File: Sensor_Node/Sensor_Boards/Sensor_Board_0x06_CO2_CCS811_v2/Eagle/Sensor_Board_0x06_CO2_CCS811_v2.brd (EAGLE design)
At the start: 55 x 35 mm, 28 parts, among them J1 M04_SMD_90, J4 ARDUINO_ISP, U1 CCS811, U2 ATMEGA328P_TQFP, Y1 8MHZ

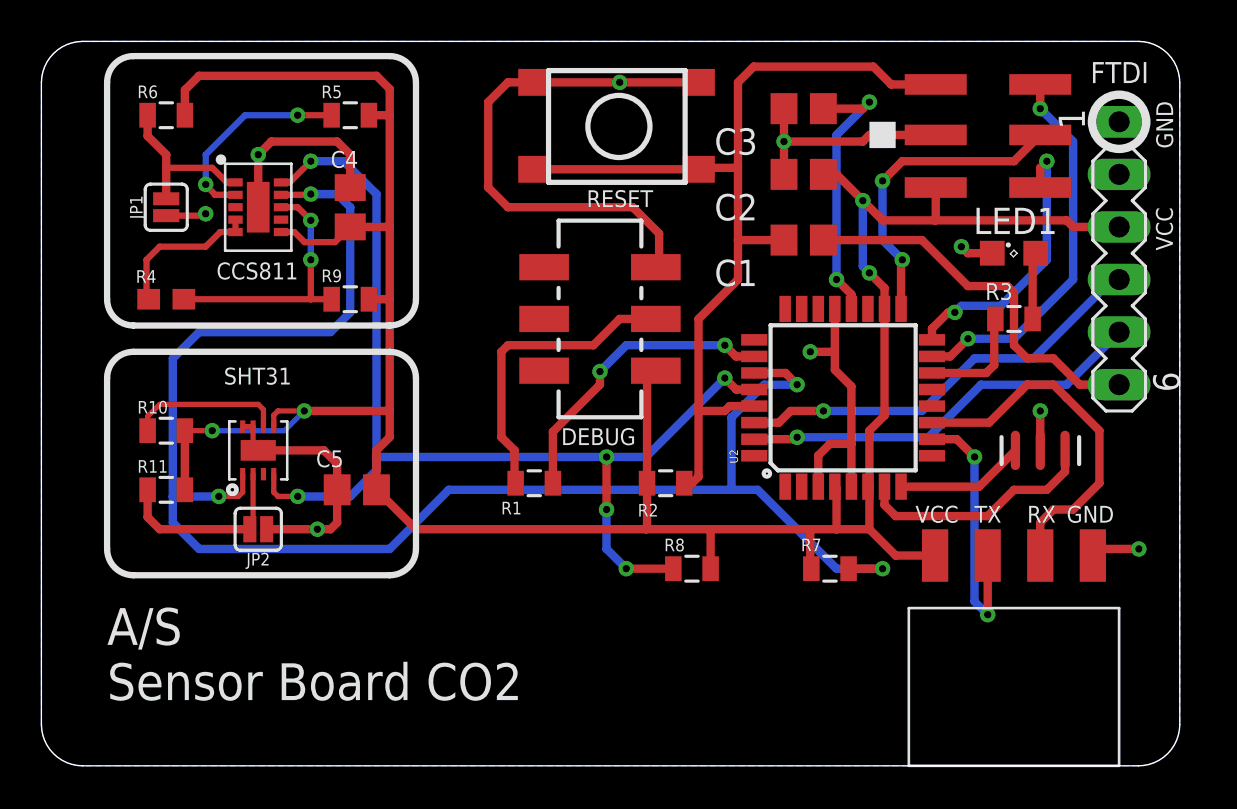
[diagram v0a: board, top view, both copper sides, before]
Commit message: Changes to C02-Board
- added power socket
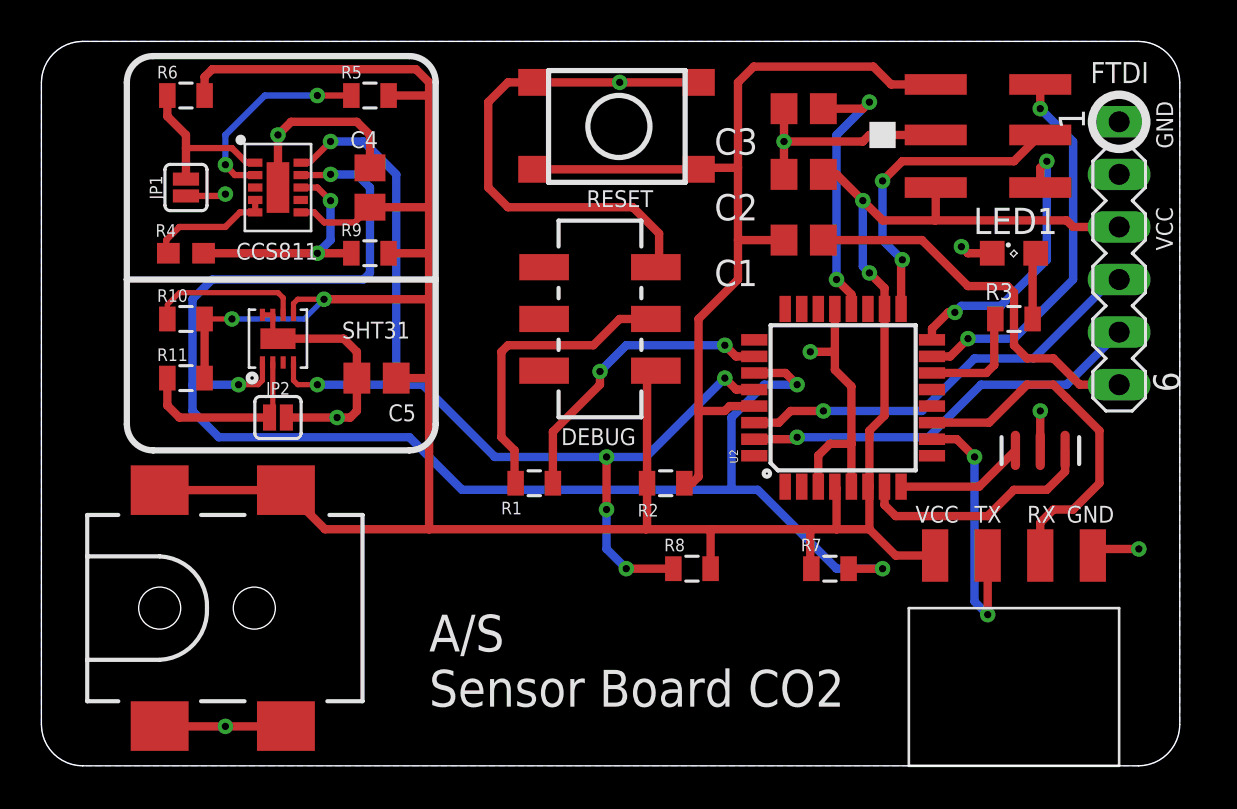
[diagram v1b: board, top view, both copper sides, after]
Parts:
- added J2: 5.5x2.1mm Barrel, wsn:POWER_JACK_SMD
- moved C5 5.48 mm to (16.2, 18.7)
- moved JP2 5.48 mm to (11.4, 16.8)
- moved R10 5.48 mm to (6.99, 21.6)
- moved R11 5.48 mm to (6.99, 18.7)
- moved U3 5.48 mm to (11.4, 20.6)
- moved R4 2.42 mm to (6.99, 24.8)
- moved R9 2.42 mm to (15.9, 24.8)
- moved C4 1.35 mm to (15.9, 27.9)
- moved JP1 1.35 mm to (6.99, 27.9)
- moved U1 1.35 mm to (11.4, 27.9)
- moved R5 1.35 mm to (15.9, 32.4)
- moved R6 1.35 mm to (6.99, 32.4)
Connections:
- net GND: now also J2.GND, J2.P$4
- net VCC: now also J2.VIN0, J2.VIN1
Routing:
- net VCC: track 130.0 -> 148.4 mm
- net GND: track 78.8 -> 84.9 mm, vias 9 -> 10
- net SDA: track 79.3 -> 74.3 mm
- net SCL: track 53.6 -> 50.4 mm
- net NTC_SENSE: track 7.70 -> 6.11 mm
- net AUX: track 12.7 -> 11.6 mm

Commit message: Changes CO2 and combined mask.
- added combined mask of all new PCBs
- rotated a cap on CO2-Board by 90°
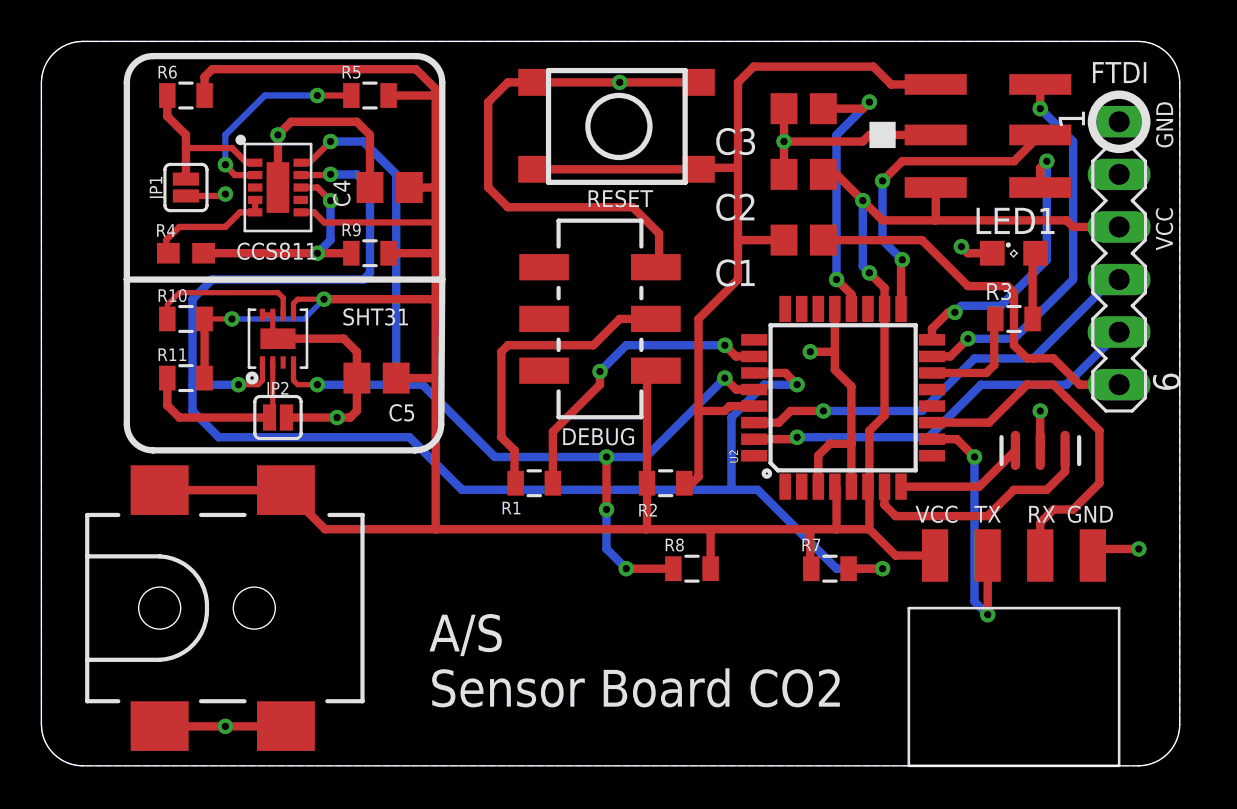
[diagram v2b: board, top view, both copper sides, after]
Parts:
- moved C4 0.95 mm to (16.8, 27.9), turned to 180 degrees
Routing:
- net VCC: track 148.4 -> 151.0 mm
- net GND: track 84.9 -> 85.9 mm
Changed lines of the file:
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@@
 <?xml version="1.0" encoding="utf-8"?>
 <!DOCTYPE eagle SYSTEM "eagle.dtd">
-<eagle version="8.5.0">
+<eagle version="8.5.2">
 <drawing>
 <settings>
@@
 <text x="29.553896875" y="27.8079125" size="0.8128" layer="21" rot="R180">RESET</text>
 <text x="28.718196875" y="16.308665625" size="0.8128" layer="21" rot="R180">DEBUG</text>
-<text x="17.806396875" y="21.4579125" size="0.8128" layer="21" rot="R180">SHT31</text>
+<text x="17.806396875" y="22.0929125" size="0.8128" layer="21" rot="R180">SHT31</text>
 <text x="13.361396875" y="25.2679125" size="0.8128" layer="21" rot="R180">CCS811</text>
 <wire x1="4.1275" y1="23.495" x2="4.1275" y2="33.02" width="0.3048" layer="21"/>
 <wire x1="4.1275" y1="33.02" x2="5.3975" y2="34.29" width="0.3048" layer="21" curve="-90"/>
-<wire x1="5.3975" y1="34.29" x2="17.78" y2="34.29" width="0.3048" layer="21"/>
-<wire x1="17.78" y1="34.29" x2="19.05" y2="33.02" width="0.3048" layer="21" curve="-90"/>
-<wire x1="19.05" y1="33.02" x2="19.05" y2="23.495" width="0.3048" layer="21"/>
+<wire x1="5.3975" y1="34.29" x2="18.0975" y2="34.29" width="0.3048" layer="21"/>
+<wire x1="18.0975" y1="34.29" x2="19.3675" y2="33.02" width="0.3048" layer="21" curve="-90"/>
+<wire x1="19.3675" y1="33.02" x2="19.3675" y2="23.495" width="0.3048" layer="21"/>
 <wire x1="4.1275" y1="23.495" x2="4.1275" y2="16.51" width="0.3048" layer="21"/>
 <wire x1="4.1275" y1="16.51" x2="5.3975" y2="15.24" width="0.3048" layer="21" curve="90"/>
-<wire x1="5.3975" y1="15.24" x2="17.78" y2="15.24" width="0.3048" layer="21"/>
-<wire x1="17.78" y1="15.24" x2="19.05" y2="16.51" width="0.3048" layer="21" curve="90"/>
-<wire x1="19.05" y1="16.51" x2="19.05" y2="23.495" width="0.3048" layer="21"/>
-<wire x1="4.1275" y1="23.495" x2="19.05" y2="23.495" width="0.3048" layer="21"/>
+<wire x1="5.3975" y1="15.24" x2="18.048621875" y2="15.24" width="0.3048" layer="21"/>
+<wire x1="18.048621875" y1="15.24" x2="19.318590625" y2="16.5010625" width="0.3048" layer="21" curve="89.596783"/>
+<wire x1="19.318590625" y1="16.5010625" x2="19.3675" y2="23.495" width="0.3048" layer="21"/>
+<wire x1="4.1275" y1="23.495" x2="19.3675" y2="23.495" width="0.3048" layer="21"/>
 </plain>
 <attributes>
@@
 <attribute name="NAME" x="14.478" y="25.5905" size="0.6096" layer="25"/>
 </element>
-<element name="C4" library="eagle-ltspice" package="C0805" value="100n" x="15.875" y="27.94" smashed="yes" rot="R90">
-<attribute name="NAME" x="14.9225" y="29.845" size="0.8128" layer="25"/>
-<attribute name="SPICEMODEL" value="NONE" x="15.875" y="27.94" size="1.778" layer="27" rot="R90" display="off"/>
-<attribute name="SPICEPREFIX" value="C" x="15.875" y="27.94" size="1.778" layer="27" rot="R90" display="off"/>
+<element name="C4" library="eagle-ltspice" package="C0805" value="100n" x="16.8275" y="27.94" smashed="yes" rot="R180">
+<attribute name="NAME" x="14.9225" y="26.9875" size="0.8128" layer="25" rot="R90"/>
+<attribute name="SPICEMODEL" value="NONE" x="16.8275" y="27.94" size="1.778" layer="27" rot="R180" display="off"/>
+<attribute name="SPICEPREFIX" value="C" x="16.8275" y="27.94" size="1.778" layer="27" rot="R180" display="off"/>
 </element>
 <element name="U3" library="Adafruit SHT31 Breakout" package="MICROBUILDER_SHT3X" value="" x="11.43" y="20.6375" smashed="yes" rot="R90">
@@
 <wire x1="12.065" y1="31.115" x2="15.24" y2="31.115" width="0.4064" layer="1"/>
 <wire x1="15.24" y1="31.115" x2="15.875" y2="30.48" width="0.4064" layer="1"/>
-<wire x1="15.875" y1="30.48" x2="15.875" y2="28.89" width="0.4064" layer="1"/>
 <wire x1="22.5425" y1="26.9875" x2="21.59" y2="27.94" width="0.4064" layer="1"/>
 <wire x1="21.59" y1="27.94" x2="21.59" y2="32.0675" width="0.4064" layer="1"/>
@@
 <wire x1="8.89" y1="1.905" x2="11.8" y2="1.905" width="0.4064" layer="1"/>
 <wire x1="11.8" y1="1.905" x2="11.815" y2="1.92" width="0.4064" layer="1"/>
+<wire x1="15.875" y1="30.48" x2="15.875" y2="27.9425" width="0.4064" layer="1"/>
+<wire x1="15.875" y1="27.9425" x2="15.8775" y2="27.94" width="0.4064" layer="1"/>
+<wire x1="52.07" y1="28.575" x2="52.07" y2="31.115" width="0" layer="19" extent="1-1"/>
+<wire x1="45.94" y1="24.765" x2="52.07" y2="28.575" width="0" layer="19" extent="1-1"/>
+<wire x1="43.21" y1="30.48" x2="44.45" y2="25.0825" width="0" layer="19" extent="1-1"/>
+<wire x1="31.7625" y1="33.02" x2="35.88" y2="31.75" width="0" layer="19" extent="1-1"/>
+<wire x1="15.8775" y1="27.94" x2="21.59" y2="27.94" width="0" layer="19" extent="1-1"/>
+<wire x1="8.89" y1="27.6225" x2="11.43" y2="27.94" width="0" layer="19" extent="1-1"/>
+<wire x1="10.68" y1="21.7875" x2="8.8011" y2="27.5336" width="0" layer="19" extent="1-1"/>
+<wire x1="38.335" y1="22.0726" x2="44.45" y2="25.0825" width="0" layer="19" extent="1-1"/>
+<wire x1="48.26" y1="17.145" x2="45.94" y2="24.765" width="0" layer="19" extent="1-1"/>
+<wire x1="51.1175" y1="10.4775" x2="48.26" y2="15.24" width="0" layer="19" extent="1-1"/>
+<wire x1="11.815" y1="1.92" x2="11.8364" y2="16.8275" width="0" layer="19" extent="1-1"/>
 </signal>
 <signal name="VCC" class="1">
@@
 <wire x1="12.18" y1="22.34" x2="12.3825" y2="22.5425" width="0.254" layer="1"/>
 <wire x1="12.3825" y1="22.5425" x2="13.6525" y2="22.5425" width="0.254" layer="1"/>
-<wire x1="15.875" y1="26.99" x2="15.8775" y2="26.9875" width="0.4064" layer="1"/>
-<wire x1="18.7325" y1="26.9875" x2="15.8775" y2="26.9875" width="0.4064" layer="1"/>
 <wire x1="32.385" y1="11.43" x2="37.1475" y2="11.43" width="0.4064" layer="1"/>
 <wire x1="37.1475" y1="11.43" x2="38.4175" y2="11.43" width="0.4064" layer="1"/>
 <wire x1="12.53" y1="26.74" x2="13.17975" y2="26.74" width="0.3048" layer="1"/>
 <wire x1="13.17975" y1="26.74" x2="13.66605" y2="26.2537" width="0.3048" layer="1"/>
-<wire x1="13.66605" y1="26.2537" x2="15.1437" y2="26.2537" width="0.3048" layer="1"/>
-<wire x1="15.1437" y1="26.2537" x2="15.8775" y2="26.9875" width="0.3048" layer="1"/>
+<wire x1="13.66605" y1="26.2537" x2="18.9537" y2="26.2537" width="0.3048" layer="1"/>
 <contactref element="R7" pad="2"/>
 <contactref element="R8" pad="2"/>
@@
 <wire x1="7.885" y1="33.285" x2="8.255" y2="33.655" width="0.4064" layer="1"/>
 <wire x1="8.255" y1="33.655" x2="18.0975" y2="33.655" width="0.4064" layer="1"/>
-<wire x1="29.21" y1="11.43" x2="18.7325" y2="11.43" width="0.4064" layer="1"/>
-<wire x1="18.7325" y1="11.43" x2="13.705" y2="11.43" width="0.4064" layer="1"/>
+<wire x1="29.21" y1="11.43" x2="19.05" y2="11.43" width="0.4064" layer="1"/>
+<wire x1="19.05" y1="11.43" x2="13.705" y2="11.43" width="0.4064" layer="1"/>
 <wire x1="13.705" y1="11.43" x2="11.815" y2="13.32" width="0.4064" layer="1"/>
 <wire x1="11.815" y1="13.32" x2="5.715" y2="13.32" width="0.4064" layer="1"/>
-<wire x1="18.0975" y1="33.655" x2="18.7325" y2="33.02" width="0.4064" layer="1"/>
-<wire x1="18.7325" y1="33.02" x2="18.7325" y2="32.385" width="0.4064" layer="1"/>
-<wire x1="18.7325" y1="32.385" x2="18.7325" y2="26.9875" width="0.4064" layer="1"/>
-<wire x1="18.7325" y1="26.9875" x2="18.7325" y2="24.765" width="0.4064" layer="1"/>
-<wire x1="18.7325" y1="24.765" x2="18.7325" y2="22.5425" width="0.4064" layer="1"/>
-<wire x1="18.7325" y1="22.5425" x2="18.7325" y2="18.7325" width="0.4064" layer="1"/>
-<wire x1="18.7325" y1="18.7325" x2="18.7325" y2="11.43" width="0.4064" layer="1"/>
-<wire x1="17.1425" y1="18.7325" x2="18.7325" y2="18.7325" width="0.4064" layer="1"/>
-<wire x1="13.6525" y1="22.5425" x2="18.7325" y2="22.5425" width="0.4064" layer="1"/>
-<wire x1="16.775" y1="24.765" x2="18.7325" y2="24.765" width="0.4064" layer="1"/>
-<wire x1="16.775" y1="32.385" x2="18.7325" y2="32.385" width="0.4064" layer="1"/>
+<wire x1="18.0975" y1="33.655" x2="19.05" y2="32.7025" width="0.4064" layer="1"/>
+<wire x1="19.05" y1="32.7025" x2="19.05" y2="32.385" width="0.4064" layer="1"/>
+<wire x1="19.05" y1="32.385" x2="19.05" y2="27.94" width="0.4064" layer="1"/>
+<wire x1="19.05" y1="27.94" x2="19.05" y2="24.765" width="0.4064" layer="1"/>
+<wire x1="19.05" y1="24.765" x2="19.05" y2="22.5425" width="0.4064" layer="1"/>
+<wire x1="19.05" y1="22.5425" x2="19.05" y2="18.7325" width="0.4064" layer="1"/>
+<wire x1="19.05" y1="18.7325" x2="19.05" y2="11.43" width="0.4064" layer="1"/>
+<wire x1="17.1425" y1="18.7325" x2="19.05" y2="18.7325" width="0.4064" layer="1"/>
+<wire x1="13.6525" y1="22.5425" x2="19.05" y2="22.5425" width="0.4064" layer="1"/>
+<wire x1="16.775" y1="24.765" x2="19.05" y2="24.765" width="0.4064" layer="1"/>
+<wire x1="16.775" y1="32.385" x2="19.05" y2="32.385" width="0.4064" layer="1"/>
+<wire x1="17.7775" y1="27.94" x2="19.05" y2="27.94" width="0.4064" layer="1"/>
+<wire x1="19.05" y1="24.765" x2="18.9537" y2="26.2537" width="0" layer="19" extent="1-1"/>
 </signal>
 <signal name="RESET">

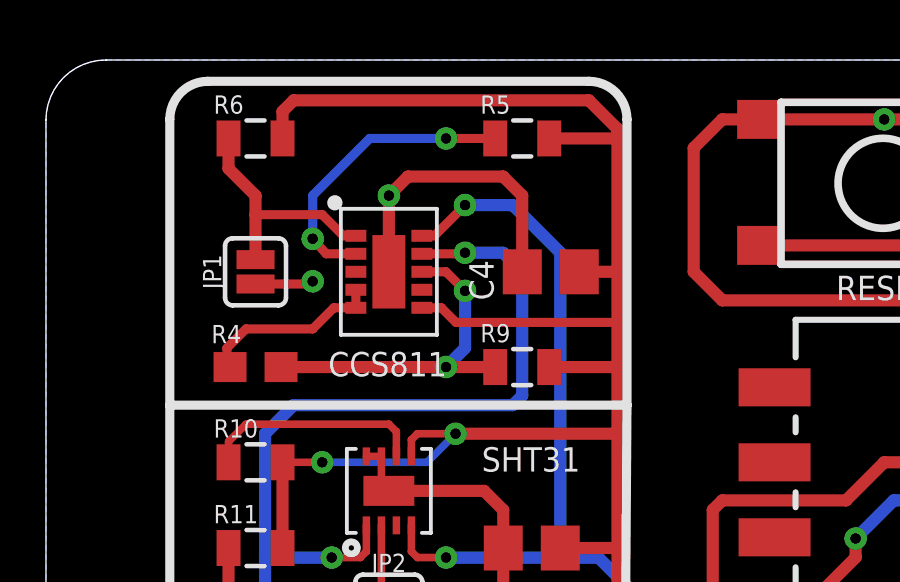
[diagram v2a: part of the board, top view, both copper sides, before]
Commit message: Corrected mistake on C02-Board
-Connected enable-pin of sensor to GND
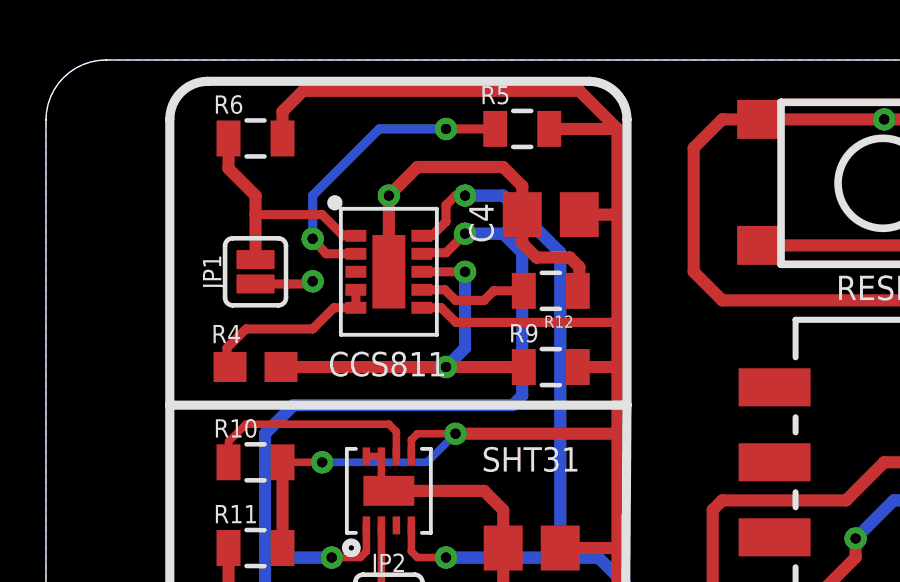
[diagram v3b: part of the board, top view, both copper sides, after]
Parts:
- added R12: 100k, SparkFun-Passives:0805
- moved C4 1.90 mm to (16.8, 29.8)
- moved R9 0.95 mm to (16.8, 24.8)
- moved R5 0.32 mm to (15.9, 32.7)
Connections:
- removed net SENS_WAKE: U1.7
- new net N$5: R12.2, U1.7
- net GND: now also R12.1
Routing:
- net N$5: track 0.00 -> 3.68 mm
- net GND: track 85.9 -> 88.4 mm
- net AUX: track 11.6 -> 13.0 mm
- net SDA: track 74.3 -> 75.2 mm
- net SCL: track 50.4 -> 51.0 mm
- net VCC: track 151.0 -> 150.4 mm

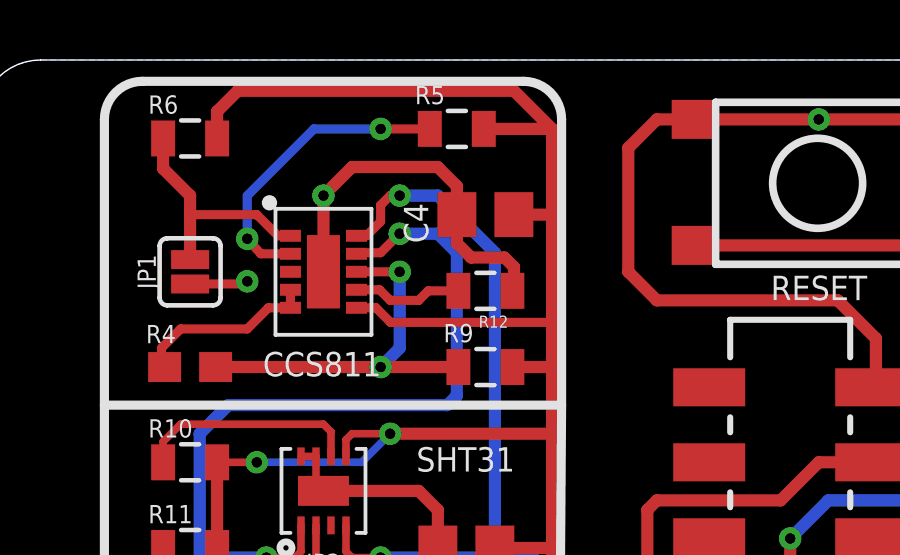
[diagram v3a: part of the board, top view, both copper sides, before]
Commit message: Various changes
- updated two masks
- changed combined mask again
- tiedied up CO2 sensor a bit
- used another footprint for TSL2561-sensor
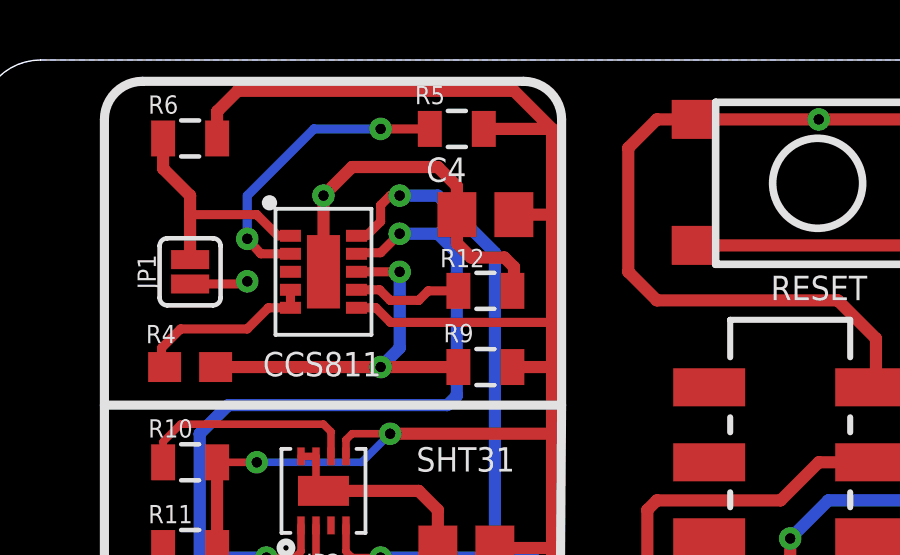
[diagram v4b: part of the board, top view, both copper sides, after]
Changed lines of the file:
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@@
 </element>
 <element name="C4" library="eagle-ltspice" package="C0805" value="100n" x="16.8275" y="29.845" smashed="yes" rot="R180">
-<attribute name="NAME" x="14.9225" y="28.8925" size="0.8128" layer="25" rot="R90"/>
+<attribute name="NAME" x="16.1925" y="31.75" size="0.8128" layer="25" rot="R180"/>
 <attribute name="SPICEMODEL" value="NONE" x="16.8275" y="29.845" size="1.778" layer="27" rot="R180" display="off"/>
 <attribute name="SPICEPREFIX" value="C" x="16.8275" y="29.845" size="1.778" layer="27" rot="R180" display="off"/>
@@
 <attribute name="SF_ID" value="PRT-12748" x="5.715" y="7.62" size="1.778" layer="27" display="off"/>
 </element>
-<element name="R12" library="SparkFun-Passives" package="0805" value="100k" x="16.8275" y="27.305" rot="R180"/>
+<element name="R12" library="SparkFun-Passives" package="0805" value="100k" x="16.8275" y="27.305" smashed="yes" rot="R180">
+<attribute name="NAME" x="16.79575" y="28.702" size="0.6096" layer="25" rot="R180"/>
+</element>
 </elements>
 <signals>
